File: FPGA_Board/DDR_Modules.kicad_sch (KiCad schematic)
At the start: 1 part

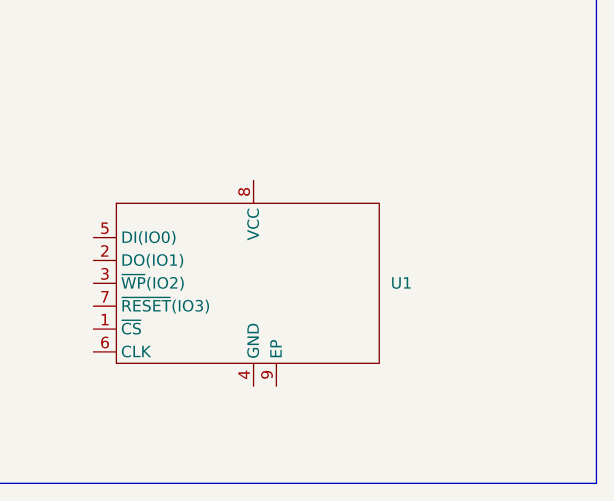
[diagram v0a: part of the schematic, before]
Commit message: Create Block Diagram, create Vivado Project
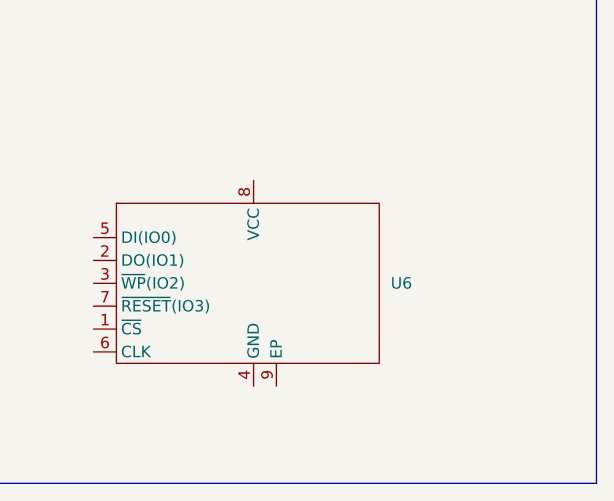
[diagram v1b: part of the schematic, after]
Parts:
- renumbered U1 to U6
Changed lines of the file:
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@@
 		(dnp no)
 		(fields_autoplaced yes)
-		(property "Reference" "U1"
+		(property "Reference" "U6"
 			(at 88.9 161.2899 0)
 			(effects
@@
 		(instances
 			(project "FPGA_Board"
-				(path "/472f09b1-9eb3-4828-aa92-3f9176530a4e/1202234b-3398-4b70-bea7-fa7b5bc7f21a"
-					(reference "U1")
+				(path "/472f09b1-9eb3-4828-aa92-3f9176530a4e/404569be-c671-46d7-9e86-2db1b2045195"
+					(reference "U6")
 					(unit 1)
 				)

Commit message: Create block diagram & QSPI footprint
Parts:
- removed U6: ~, Package_SON:WSON-8-1EP_8x6mm_P1.27mm_EP3.4x4.3mm, symbol FPGA_Parts:W25Q128JVEIQ
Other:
- note removed: "QSPI INTERFACE"
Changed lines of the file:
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@@
 		(company "AUSTIN ADAM")
 	)
-	(rectangle
-		(start 27.94 127.635)
-		(end 111.76 183.515)
-		(stroke
-			(width 0)
-			(type default)
-		)
-		(fill
-			(type none)
-		)
-	)
-	(text "QSPI INTERFACE"
-		(exclude_from_sim no)
-		(at 43.942 124.968 0)
-		(effects
-			(font
-				(size 2.54 2.54)
-				(thickness 0.762)
-				(bold yes)
-			)
-		)
-	)
-	(symbol
-		(lib_id "FPGA_Parts:W25Q128JVEIQ")
-		(at 72.39 161.29 0)
-		(unit 1)
-		(exclude_from_sim no)
-		(in_bom yes)
-		(on_board yes)
-		(dnp no)
-		(fields_autoplaced yes)
-		(property "Reference" "U6"
-			(at 88.9 161.2899 0)
-			(effects
-				(font
-					(size 1.27 1.27)
-				)
-				(justify left)
-			)
-		)
-		(property "Value" "~"
-			(at 72.39 161.29 0)
-			(effects
-				(font
-					(size 1.27 1.27)
-				)
-				(hide yes)
-			)
-		)
-		(property "Footprint" "Package_SON:WSON-8-1EP_8x6mm_P1.27mm_EP3.4x4.3mm"
-			(at 67.056 144.018 0)
-			(effects
-				(font
-					(size 1.27 1.27)
-				)
-				(hide yes)
-			)
-		)
-		(property "Datasheet" "https://www.winbond.com/resource-files/w25q128jv%20revf%2003272018%20plus.pdf"
-			(at 72.39 161.29 0)
-			(effects
-				(font
-					(size 1.27 1.27)
-				)
-				(hide yes)
-			)
-		)
-		(property "Description" "NOR Flash spiFlash, 3V, 128M-bit, 4Kb Uniform Sector"
-			(at 66.04 141.224 0)
-			(effects
-				(font
-					(size 1.27 1.27)
-				)
-				(hide yes)
-			)
-		)
-		(pin "5"
-		)
-		(pin "6"
-		)
-		(pin "4"
-		)
-		(pin "9"
-		)
-		(pin "2"
-		)
-		(pin "3"
-		)
-		(pin "7"
-		)
-		(pin "1"
-		)
-		(pin "8"
-		)
-		(instances
-			(project "FPGA_Board"
-				(path "/472f09b1-9eb3-4828-aa92-3f9176530a4e/404569be-c671-46d7-9e86-2db1b2045195"
-					(reference "U6")
-					(unit 1)
-				)
-			)
-		)
-	)
 )

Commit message: add FPGA,DDR, Decoupling capacitor symbols for power & ddr sheets. modify symbols pinout placement to clean up schematic
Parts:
- added U3, U4: MT41K256M16TW, Package_BGA:Micron_FBGA-96_8x14mm_Layout9x16_P0.8mm, symbol Memory_RAM:MT41K256M16TW
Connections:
- new net: U3.A1 (V_{DDQ}), U3.A8 (V_{DDQ}), U3.C1 (V_{DDQ}), U3.C9 (V_{DDQ}), U3.D2 (V_{DDQ}), U3.E9 (V_{DDQ}), U3.F1 (V_{DDQ}), U3.H2 (V_{DDQ}), U3.H9 (V_{DDQ})
- new net: U3.A9 (V_{SS}), U3.B3 (V_{SS}), U3.E1 (V_{SS}), U3.G8 (V_{SS}), U3.J2 (V_{SS}), U3.J8 (V_{SS}), U3.M1 (V_{SS}), U3.M9 (V_{SS}), U3.P1 (V_{SS}), U3.P9 (V_{SS}), U3.T1 (V_{SS}), U3.T9 (V_{SS})
- new net: U3.B1 (V_{SSQ}), U3.B9 (V_{SSQ}), U3.D1 (V_{SSQ}), U3.D8 (V_{SSQ}), U3.E2 (V_{SSQ}), U3.E8 (V_{SSQ}), U3.F9 (V_{SSQ}), U3.G1 (V_{SSQ}), U3.G9 (V_{SSQ})
- new net: U3.B2 (V_{DD}), U3.D9 (V_{DD}), U3.G7 (V_{DD}), U3.K2 (V_{DD}), U3.K8 (V_{DD}), U3.N1 (V_{DD}), U3.N9 (V_{DD}), U3.R1 (V_{DD}), U3.R9 (V_{DD})
- new net: U4.A1 (V_{DDQ}), U4.A8 (V_{DDQ}), U4.C1 (V_{DDQ}), U4.C9 (V_{DDQ}), U4.D2 (V_{DDQ}), U4.E9 (V_{DDQ}), U4.F1 (V_{DDQ}), U4.H2 (V_{DDQ}), U4.H9 (V_{DDQ})
- new net: U4.A9 (V_{SS}), U4.B3 (V_{SS}), U4.E1 (V_{SS}), U4.G8 (V_{SS}), U4.J2 (V_{SS}), U4.J8 (V_{SS}), U4.M1 (V_{SS}), U4.M9 (V_{SS}), U4.P1 (V_{SS}), U4.P9 (V_{SS}), U4.T1 (V_{SS}), U4.T9 (V_{SS})
- new net: U4.B1 (V_{SSQ}), U4.B9 (V_{SSQ}), U4.D1 (V_{SSQ}), U4.D8 (V_{SSQ}), U4.E2 (V_{SSQ}), U4.E8 (V_{SSQ}), U4.F9 (V_{SSQ}), U4.G1 (V_{SSQ}), U4.G9 (V_{SSQ})
- new net: U4.B2 (V_{DD}), U4.D9 (V_{DD}), U4.G7 (V_{DD}), U4.K2 (V_{DD}), U4.K8 (V_{DD}), U4.N1 (V_{DD}), U4.N9 (V_{DD}), U4.R1 (V_{DD}), U4.R9 (V_{DD})
